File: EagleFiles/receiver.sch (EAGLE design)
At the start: 3 parts, among them IC1 MEGA8-AI

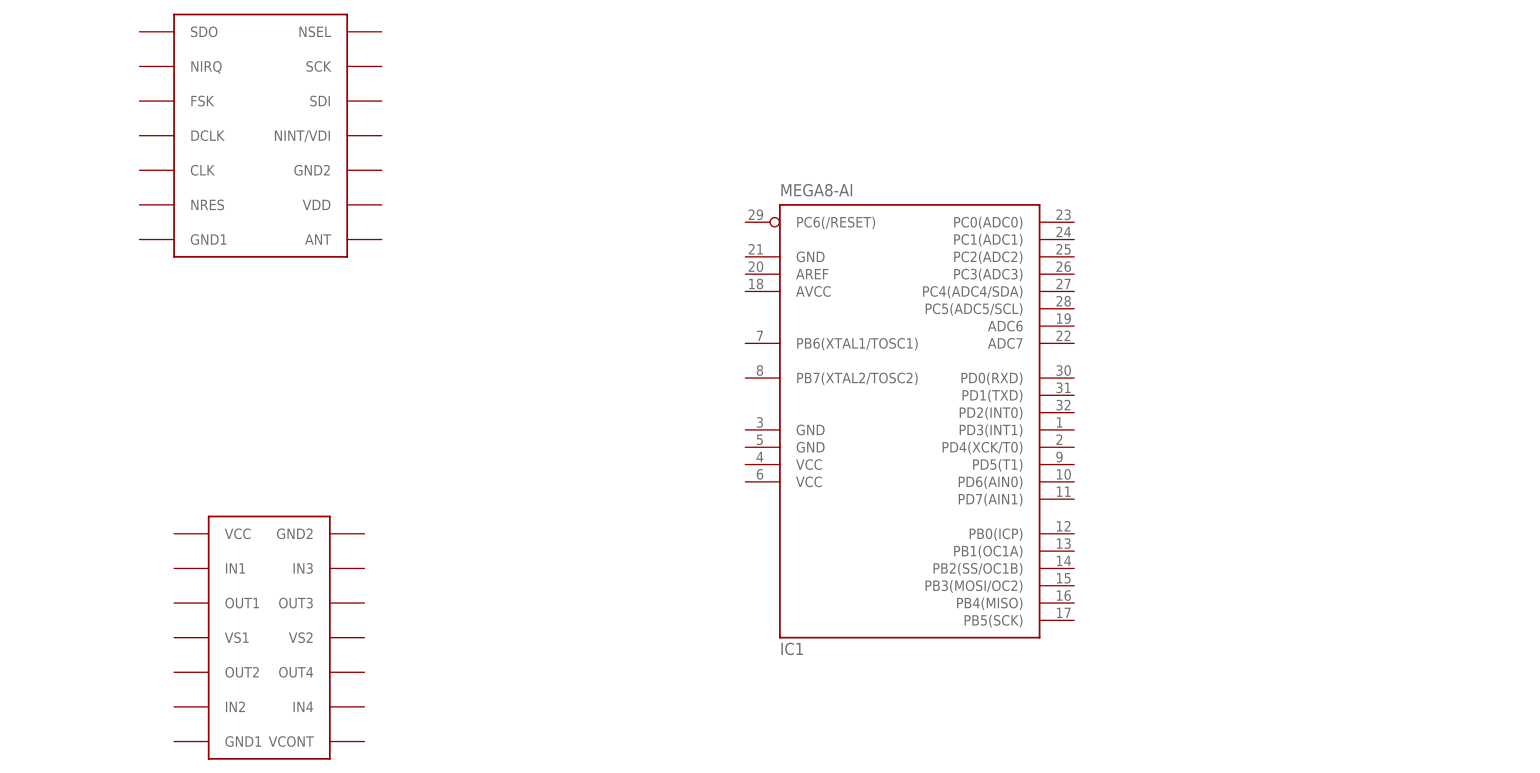
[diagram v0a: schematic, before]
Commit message: Added eagle files for LB1836M breakout board and unfinished receiver
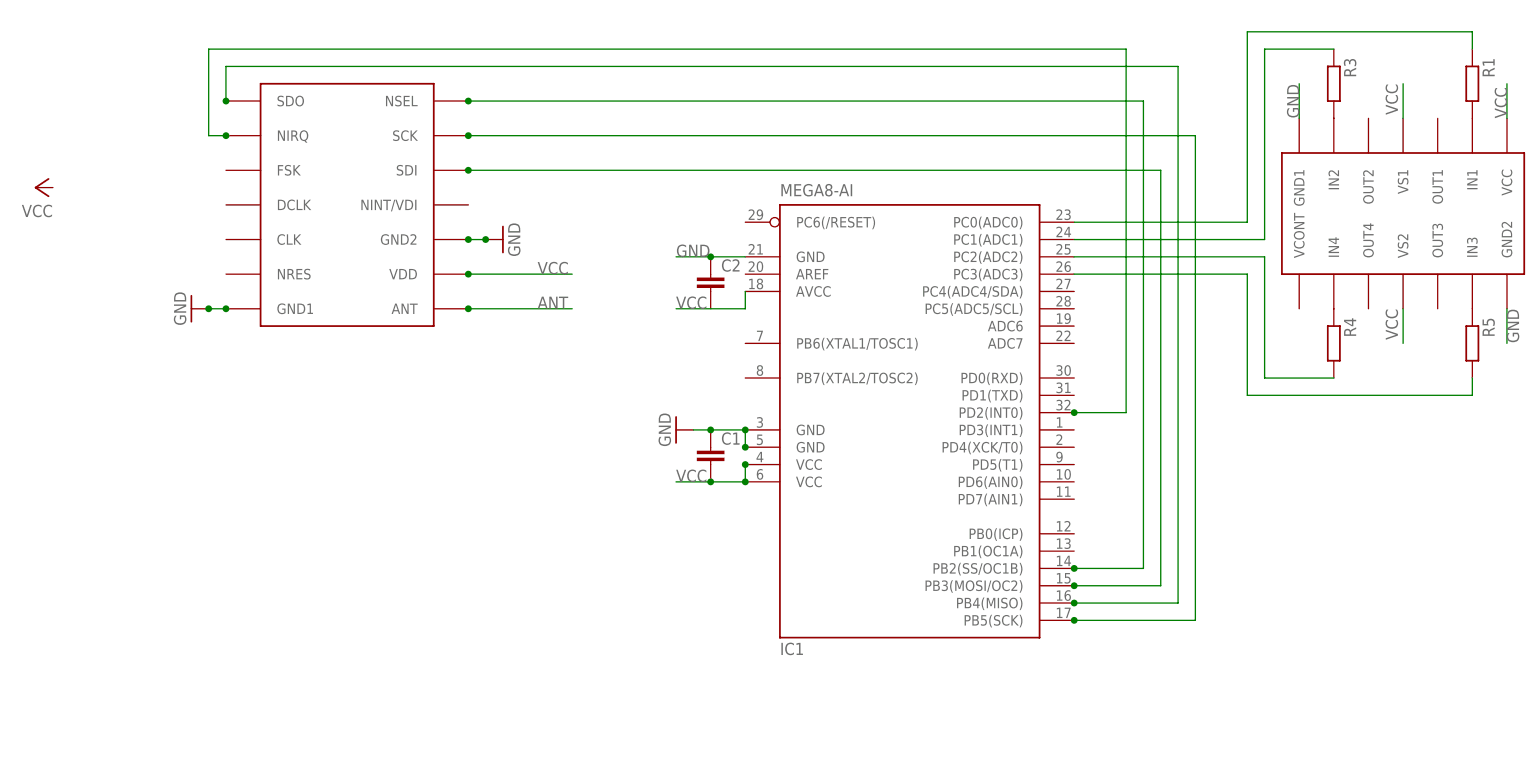
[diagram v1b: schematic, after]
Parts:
- added C1, C2: (no value), resistor:C-EUC0805
- added R1, R3, R4, R5: (no value), resistor:R-EU_R2012
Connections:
- new net ANT: RFM12B.ANT
- new net GND: C1.1, C2.1, IC1.GND, IC1.GND@1, IC1.GND@2, LB1836M.GND1, LB1836M.GND2, RFM12B.GND1, RFM12B.GND2
- new net N$1: IC1.PB4(MISO), RFM12B.SDO
- new net N$10: LB1836M.IN3, R5.1
- new net N$11: IC1.PC1(ADC1), R3.1
- new net N$12: IC1.PC2(ADC2), R4.2
- new net N$13: IC1.PC3(ADC3), R5.2
- new net N$2: IC1.PB3(MOSI/OC2), RFM12B.SDI
- new net N$3: IC1.PB5(SCK), RFM12B.SCK
- new net N$4: IC1.PB2(SS/OC1B), RFM12B.NSEL
- new net N$5: IC1.PD2(INT0), RFM12B.NIRQ
- new net N$6: LB1836M.IN1, R1.2
- new net N$7: IC1.PC0(ADC0), R1.1
- new net N$8: LB1836M.IN2, R3.2
- new net N$9: LB1836M.IN4, R4.1
- new net VCC: C1.2, IC1.AVCC, IC1.VCC@1, IC1.VCC@2, LB1836M.VCC, LB1836M.VS1, LB1836M.VS2, RFM12B.VDD
